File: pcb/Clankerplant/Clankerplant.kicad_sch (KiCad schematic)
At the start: 21 parts, among them J1 flash, J3 LCD screen, J4 water pump, Q2 AO3400A (mosfet), U2 ESP32-S3, Y1 40MHz

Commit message: batt
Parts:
- added BT1: Battery_Cell, symbol Device:Battery_Cell
- added C12: 1uF-10uF, symbol Device:C
- added C13, C14: 4.7-47uF, symbol Device:C
- added R1, R4: 1k-100k, symbol Device:R_US
- added R3: 1.13k (can change idk yet), symbol Device:R_US
- added U1: BQ24074RGTR, BQ24074RGTR:QFN50P300X300X100-17N, symbol BQ24074RGTR:BQ24074RGTR
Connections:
- net +3.3V is gone; now on net +3V3: C1.1, C2.1, C4.1, C5.1, C6.1, L1.2, U2.55 (VDDA), U2.56 (VDDA)
- net +3V3: now also C14.1, U1.10 (OUT_10), U1.11 (OUT_11)
- net GND: now also C12.2, C14.2, R3.1, U1.17 (EXP), U1.4 (~{CE}), U1.8 (VSS)
- net GPIO17: now also R4.2
- net GPIO18: now also R1.2
- new net: C13.1, U1.3 (BAT_3)
- new net: BT1.1 (+), C13.2
- new net: R4.1, U1.7 (~{PGOOD})
- new net: BT1.2 (-), U1.1 (TS)
- new net: R1.1, U1.9 (~{CHG})
- new net: R3.2, U1.16 (ISET)
- new net: C12.1, U1.13 (IN)
- no-connect marks 29 -> 31
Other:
- note added: "en1 and 2 is mystery to me as well as ilim for now"
- note added: "some of these are meant to be cermanic i lowk forgot thats a later issue"
- note added: "usb port somewhere"
- note added: "use impedence + PU/PD to see if charging or not"

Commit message: jul4th battery
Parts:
- added R5: 3k, symbol Device:R_US
- added U3: TPS63900DSKR, IC_TPS63900DSKR:IC_TPS63900DSKR, symbol TPS63900DSKR:TPS63900DSKR
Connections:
- net +3V3: no longer C14.1, U1.10 (OUT_10), U1.11 (OUT_11)
- net GND: now also U1.5 (EN2), R5.2
- net at C13.1, U1.3 (BAT_3): now also U1.2 (BAT_2)
- net at U1.12 (ILIM): now also R5.1
- net VSYS: now reaches U1.6 (EN1)
- net VSYS: now also C14.1, U1.10 (OUT_10), U1.11 (OUT_11)

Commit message: 4th of july again
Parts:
- added L3: 2.2 uH, symbol Device:L
- added R6: 16.2 kΩ, symbol Device:R_US
- added R7: 0 Ω, symbol Device:R_US
- added R8: 36.5 kΩ, symbol Device:R_US
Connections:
- net GND: now also R6.2, R7.1, R8.1
- net at U3.3 (CFG1): now also R8.2
- net at U3.4 (CFG2): now also R7.2
- net at U3.5 (CFG3): now also R6.1
- net at U3.7 (LX2): now also L3.2
- net at U3.9 (LX1): now also L3.1
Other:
- note removed: "en1 and 2 is mystery to me as well as ilim for now"
- moved on the sheet: U3

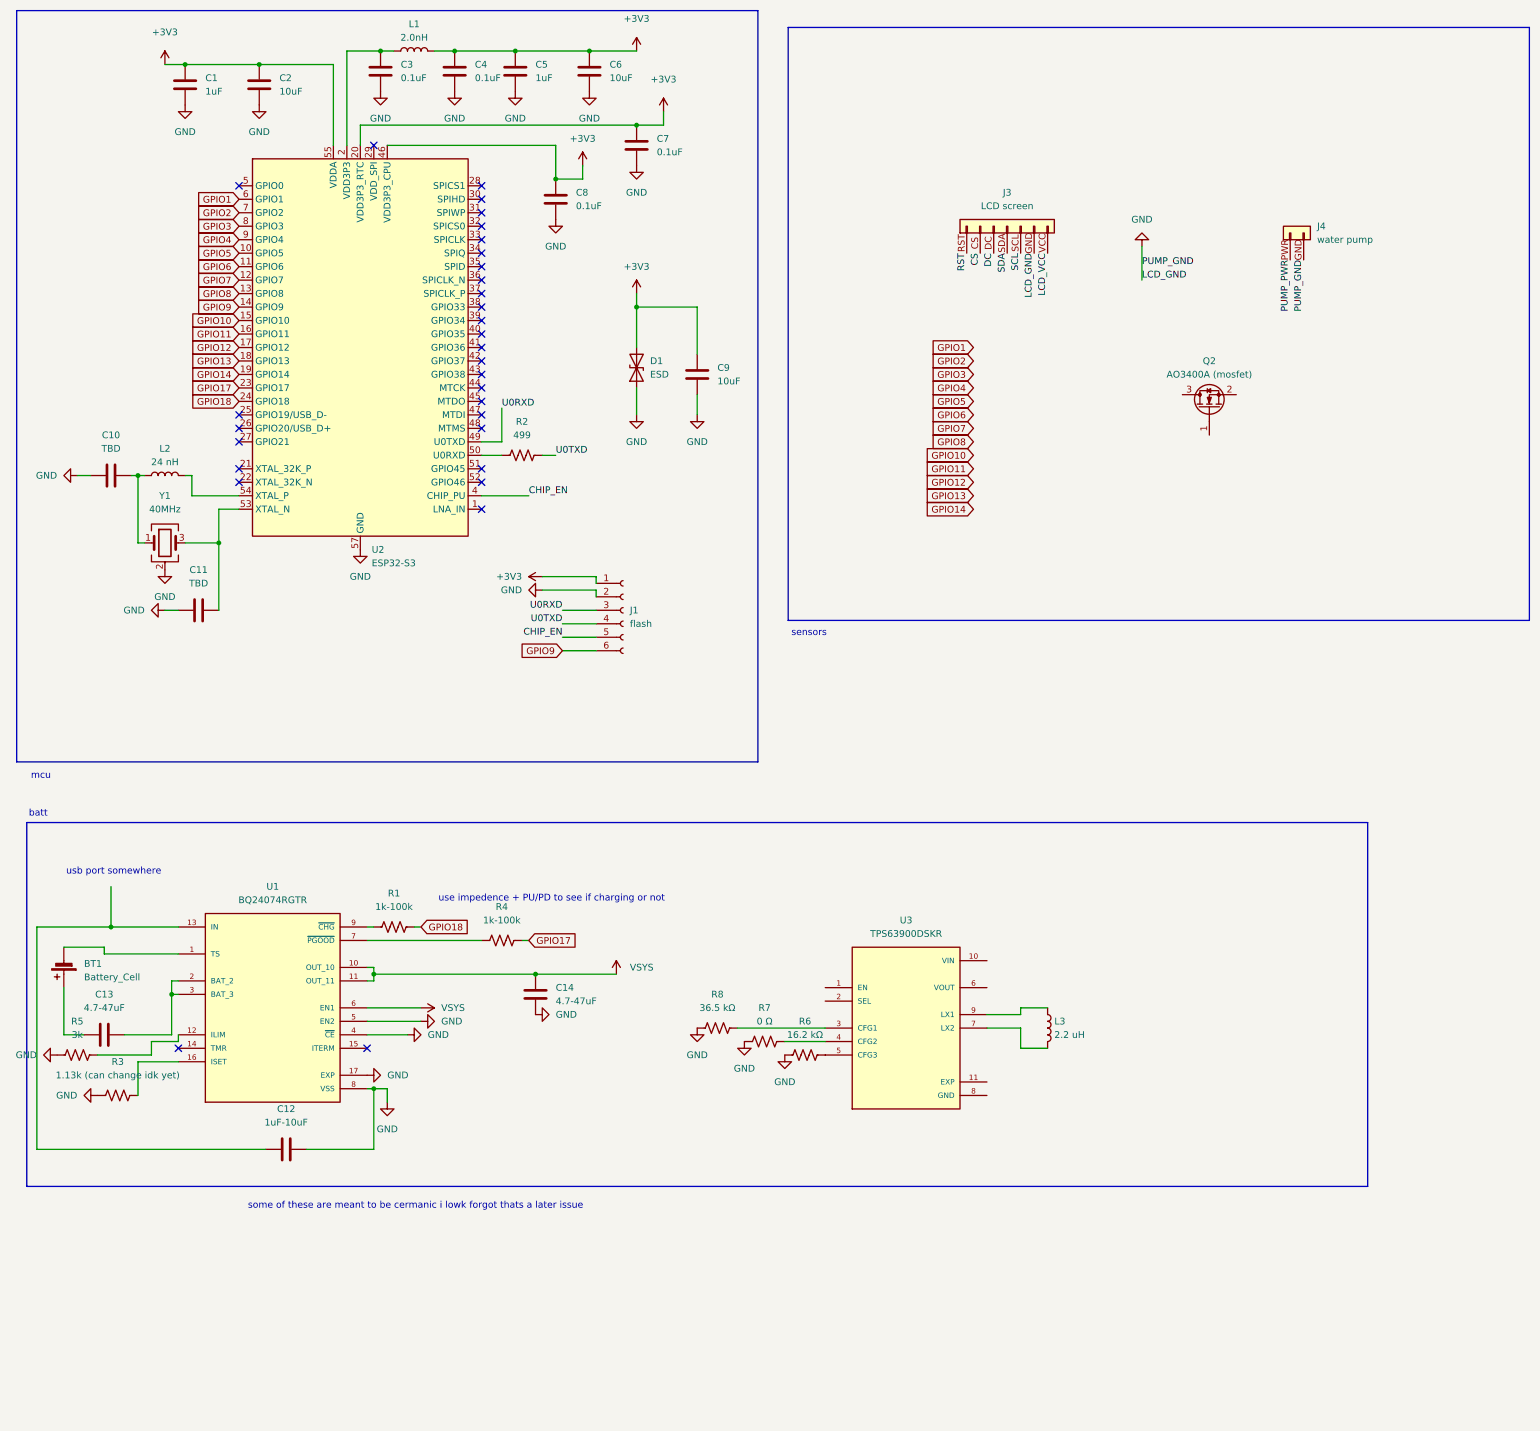
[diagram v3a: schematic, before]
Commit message: forgot to update schematci
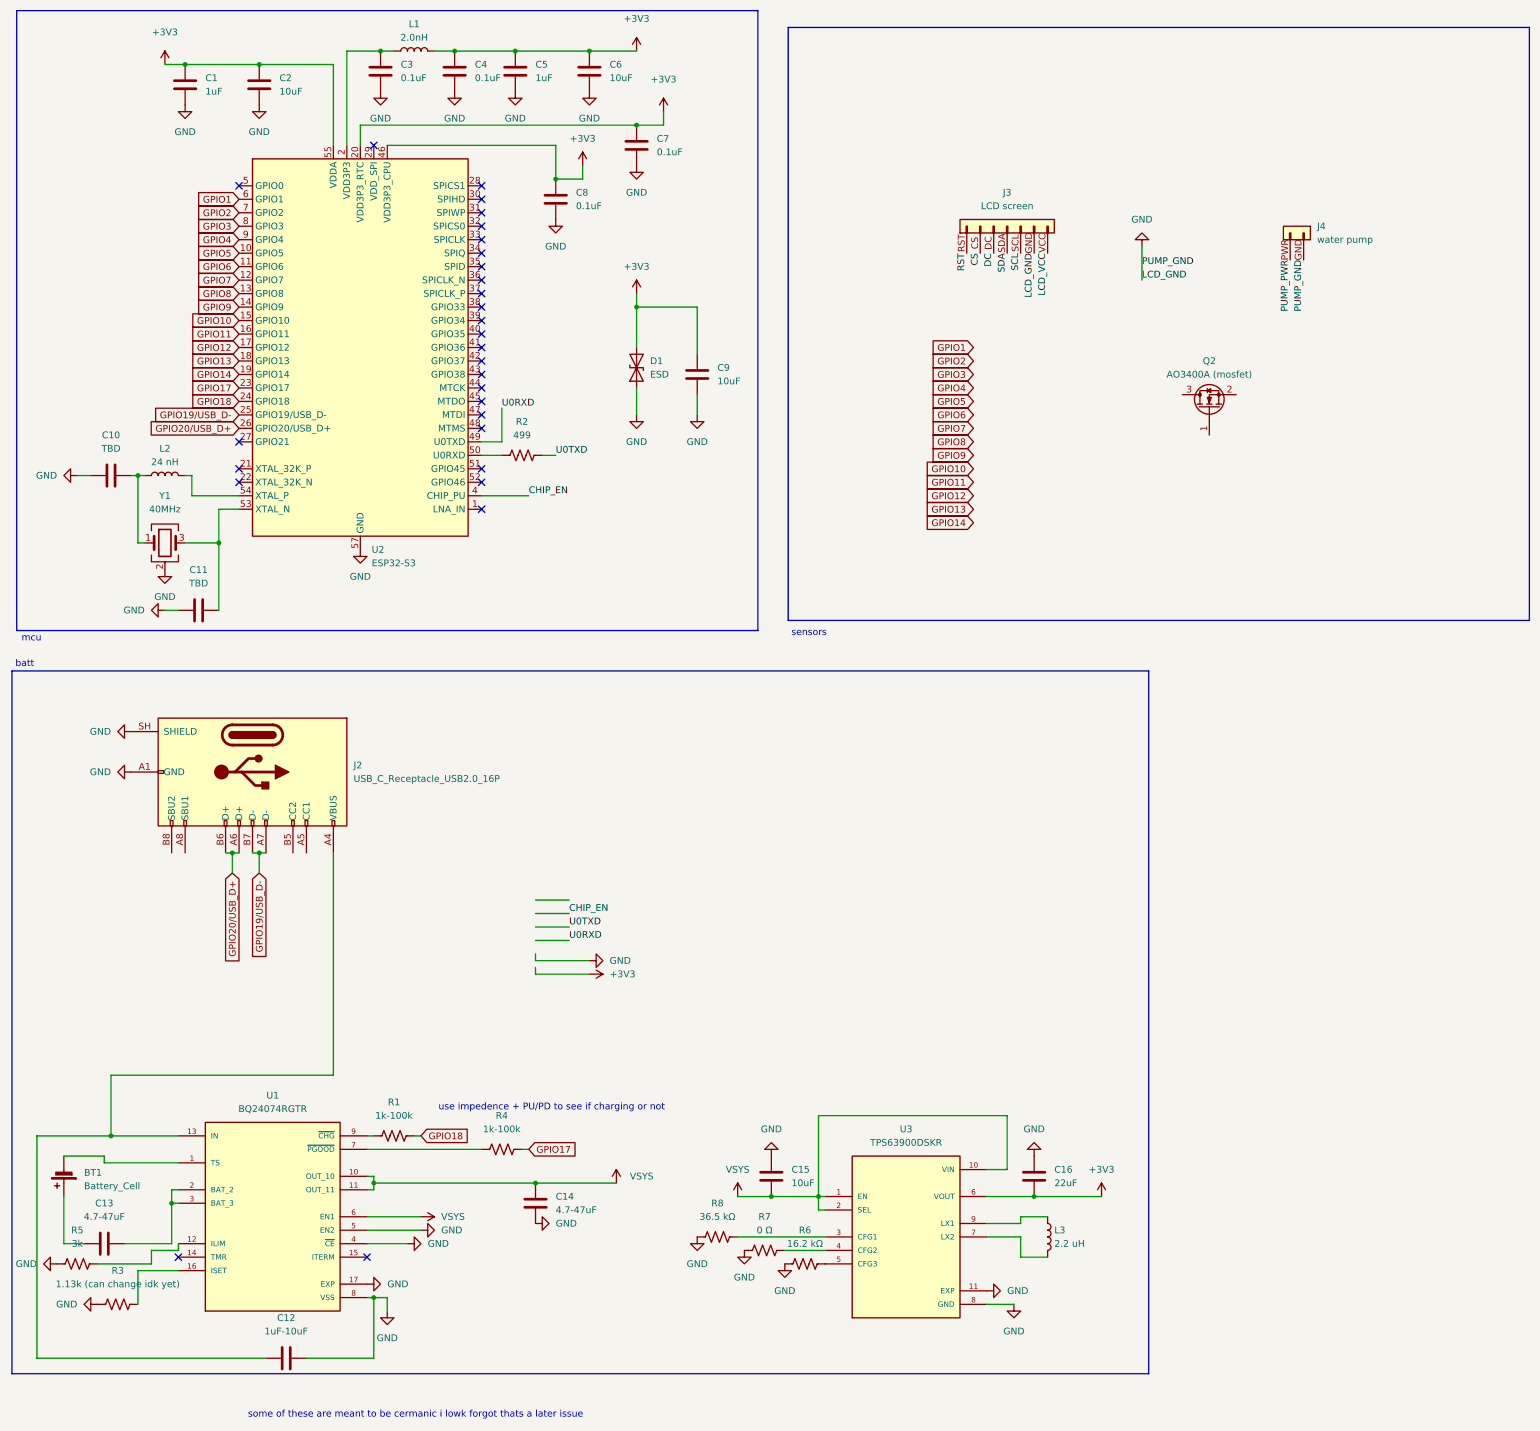
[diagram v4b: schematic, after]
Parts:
- removed J1: flash, symbol Connector:Conn_01x06_Socket
- added C15: 10uF, symbol Device:C
- added C16: 22uF, symbol Device:C
- added J2: USB_C_Receptacle_USB2.0_16P, symbol Connector:USB_C_Receptacle_USB2.0_16P
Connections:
- net +3V3: now also U3.6 (VOUT), C16.2
- net GND: now also U3.11 (EXP), U3.8 (GND), C15.1, C16.1, J2.A1 (GND), J2.A12 (GND), J2.B1 (GND), J2.B12 (GND), J2.SH (SHIELD)
- net VSYS: now also U3.1 (EN), U3.10 (VIN), U3.2 (SEL), C15.2
- net GPIO19/USB_D-: now reaches U2.25 (GPIO19/USB_D-)
- net GPIO19/USB_D-: now also J2.A7 (D-), J2.B7 (D-)
- net GPIO20/USB_D+: now reaches U2.26 (GPIO20/USB_D+)
- net GPIO20/USB_D+: now also J2.A6 (D+), J2.B6 (D+)
- net at C12.1, U1.13 (IN): now also J2.A4 (VBUS), J2.A9 (VBUS), J2.B4 (VBUS), J2.B9 (VBUS)
- no-connect marks 31 -> 29
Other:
- note removed: "usb port somewhere"
- moved on the sheet: BT1, C12, C13, C14, L3, R1, R3, R4, R5, R6, R7, R8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

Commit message: final commit :D
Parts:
- added J1: Conn_01x02, symbol Connector_Generic:Conn_01x02
- added SW1: SW_Push, symbol Switch:SW_Push
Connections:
- net GND: now also SW1.1
- net U0RXD: now also J1.1 (Pin_1)
- net U0TXD: now also J1.2 (Pin_2)
- net GPIO0: now reaches U2.5 (GPIO0)
- net GPIO0: now also SW1.2
- no-connect marks 29 -> 28
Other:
- note added: "this needs to be fixed idk what todo with it if im not using it time to go back to datasheet"
- note added: "upload"
